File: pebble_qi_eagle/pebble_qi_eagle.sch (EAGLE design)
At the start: 16 parts

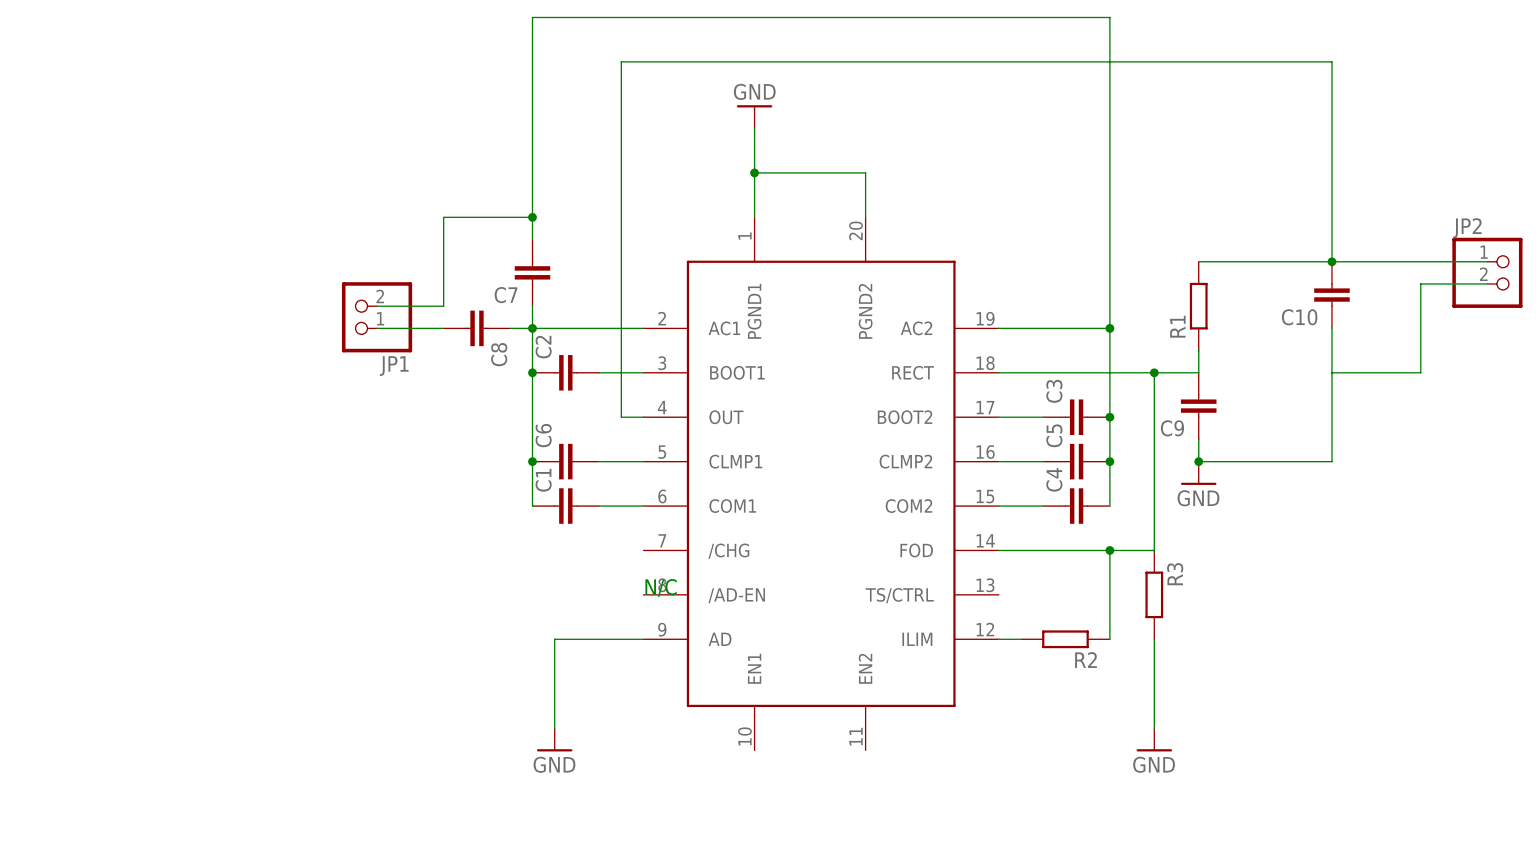
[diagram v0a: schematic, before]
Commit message: Updated schematic with values and updated read me
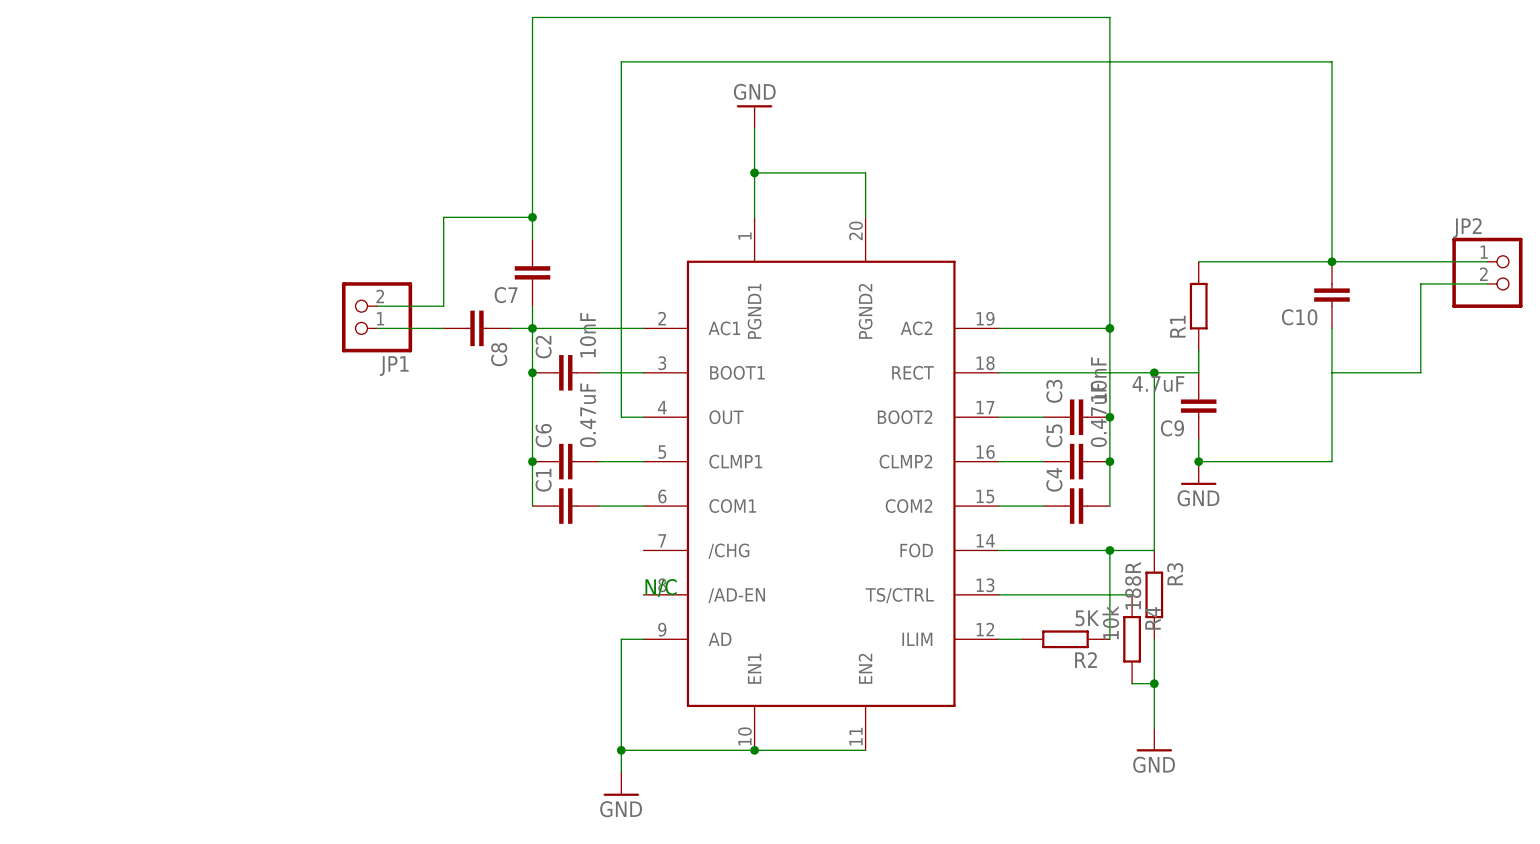
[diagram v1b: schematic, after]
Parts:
- added R4: 10k, resistor:R-EU_R0805
- C2, C3: value (none) -> 10nF
- C5, C6: value (none) -> 0.47uF
- C9: value (none) -> 4.7uF
- R2: value (none) -> 5K
- R3: value (none) -> 188R
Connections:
- new net N$6: R4.1, U$1.TS/CTRL
- net GND: now also R4.2, U$1.EN1, U$1.EN2
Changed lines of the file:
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@@
 <part name="GND2" library="supply1" deviceset="GND" device=""/>
 <part name="C1" library="resistor" deviceset="C-EU" device="C0805"/>
-<part name="C2" library="resistor" deviceset="C-EU" device="C0805"/>
-<part name="C3" library="resistor" deviceset="C-EU" device="C0805"/>
+<part name="C2" library="resistor" deviceset="C-EU" device="C0805" value="10nF"/>
+<part name="C3" library="resistor" deviceset="C-EU" device="C0805" value="10nF"/>
 <part name="C4" library="resistor" deviceset="C-EU" device="C0805"/>
-<part name="C5" library="resistor" deviceset="C-EU" device="C0805"/>
-<part name="C6" library="resistor" deviceset="C-EU" device="C0805"/>
+<part name="C5" library="resistor" deviceset="C-EU" device="C0805" value="0.47uF"/>
+<part name="C6" library="resistor" deviceset="C-EU" device="C0805" value="0.47uF"/>
 <part name="C7" library="resistor" deviceset="C-EU" device="C0805"/>
 <part name="JP1" library="pinhead" deviceset="PINHD-1X2" device="/90"/>
 <part name="C8" library="resistor" deviceset="C-EU" device="C0805"/>
 <part name="GND3" library="supply1" deviceset="GND" device=""/>
-<part name="C9" library="resistor" deviceset="C-EU" device="C0805"/>
+<part name="C9" library="resistor" deviceset="C-EU" device="C0805" value="4.7uF"/>
 <part name="R1" library="resistor" deviceset="R-EU_" device="R0805"/>
 <part name="C10" library="resistor" deviceset="C-EU" device="C0805"/>
 <part name="JP2" library="pinhead" deviceset="PINHD-1X2" device="/90"/>
-<part name="R2" library="resistor" deviceset="R-EU_" device="R0805"/>
-<part name="R3" library="resistor" deviceset="R-EU_" device="R0805"/>
+<part name="R2" library="resistor" deviceset="R-EU_" device="R0805" value="5K"/>
+<part name="R3" library="resistor" deviceset="R-EU_" device="R0805" value="188R"/>
 <part name="GND4" library="supply1" deviceset="GND" device=""/>
+<part name="R4" library="resistor" deviceset="R-EU_" device="R0805" value="10k"/>
 </parts>
 <sheets>
@@
 <instances>
 <instance part="U$1" gate="G$1" x="78.74" y="50.8"/>
-<instance part="GND1" gate="1" x="48.26" y="20.32"/>
+<instance part="GND1" gate="1" x="55.88" y="15.24"/>
 <instance part="GND2" gate="1" x="71.12" y="93.98" rot="R180"/>
 <instance part="C1" gate="G$1" x="48.26" y="48.26" rot="R90"/>
@@
 <instance part="R3" gate="G$1" x="116.84" y="38.1" rot="R270"/>
 <instance part="GND4" gate="1" x="116.84" y="20.32"/>
+<instance part="R4" gate="G$1" x="114.3" y="33.02" rot="R270"/>
 </instances>
 <busses>
@@
 <pinref part="U$1" gate="G$1" pin="AD"/>
 <pinref part="GND1" gate="1" pin="GND"/>
-<wire x1="58.42" y1="33.02" x2="48.26" y2="33.02" width="0.1524" layer="91"/>
-<wire x1="48.26" y1="33.02" x2="48.26" y2="22.86" width="0.1524" layer="91"/>
+<wire x1="58.42" y1="33.02" x2="55.88" y2="33.02" width="0.1524" layer="91"/>
+<wire x1="55.88" y1="33.02" x2="55.88" y2="20.32" width="0.1524" layer="91"/>
+<pinref part="U$1" gate="G$1" pin="EN2"/>
+<wire x1="55.88" y1="20.32" x2="55.88" y2="17.78" width="0.1524" layer="91"/>
+<wire x1="83.82" y1="20.32" x2="71.12" y2="20.32" width="0.1524" layer="91"/>
+<junction x="55.88" y="20.32"/>
+<pinref part="U$1" gate="G$1" pin="EN1"/>
+<junction x="71.12" y="20.32"/>
+<wire x1="71.12" y1="20.32" x2="55.88" y2="20.32" width="0.1524" layer="91"/>
 </segment>
 <segment>
@@
 <pinref part="GND4" gate="1" pin="GND"/>
 <pinref part="R3" gate="G$1" pin="2"/>
-<wire x1="116.84" y1="22.86" x2="116.84" y2="33.02" width="0.1524" layer="91"/>
+<wire x1="116.84" y1="22.86" x2="116.84" y2="27.94" width="0.1524" layer="91"/>
+<pinref part="R4" gate="G$1" pin="2"/>
+<wire x1="116.84" y1="27.94" x2="116.84" y2="33.02" width="0.1524" layer="91"/>
+<wire x1="114.3" y1="27.94" x2="116.84" y2="27.94" width="0.1524" layer="91"/>
+<junction x="116.84" y="27.94"/>
 </segment>
 </net>
@@
 </segment>
 </net>
+<net name="N$6" class="0">
+<segment>
+<pinref part="R4" gate="G$1" pin="1"/>
+<pinref part="U$1" gate="G$1" pin="TS/CTRL"/>
+<wire x1="114.3" y1="38.1" x2="99.06" y2="38.1" width="0.1524" layer="91"/>
+</segment>
+</net>

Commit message: Created starter board layout
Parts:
- removed JP1: (no value), pinhead:PINHD-1X2/90
- added U$2: INDUCTORCOILCRAFT_XFL3012, Ava:INDUCTORCOILCRAFT_XFL3012
- C1, C10, C3, C4, C5, C6, C7, C8, C9: device resistor:C-EUC0805 -> rcl:C-EUC0603
- C2: device resistor:C-EUC0805 -> resistor:C-EUC0603
- R1, R2, R3, R4: device resistor:R-EU_R0805 -> resistor:R-EU_R0603
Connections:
- net N$1: now also U$2.2; no longer JP1.2
- net N$7: now also U$2.1; no longer JP1.1
